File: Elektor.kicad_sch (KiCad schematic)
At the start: 55 parts, among them J1 Conn_Coaxial, J13 Conn_Coaxial, J6 Conn_01x03_Pin, J8 Conn_01x02, Q1 BF545B, U1 Si5351A-B-GT, U2 74HC04, U3 74HC4066D_653, U5 MCP6022, U6 AUDIOSHIELD-REVD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

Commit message: alternative layout first commit
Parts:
- added C20: 100n, Capacitor_SMD:C_0603_1608Metric, symbol Device:C
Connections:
- net GND: now also C20.2
- net at C16.1, R5.1, U2.14 (VCC)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: now also U2.1, U2.3, C20.1; no longer U2.11, U2.13
- net at U1.10 (CLK0), U3.5 (2E): now also U2.13; no longer U2.1
- net at U2.2: no longer U3.13 (1E)
- net at U1.9 (CLK1), U3.6 (3E): now also U2.11; no longer U2.3
- net at U2.4: no longer U3.12 (4E)
- net at U2.12: now also U3.13 (1E)
- net at U2.10: now also U3.12 (4E)
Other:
- moved on the sheet: U2A, U2B, U2E, U2F
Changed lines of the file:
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@@
   (junction (at 93.98 146.05) (diameter 0) (color 0 0 0 0)
   )
+  (junction (at 69.85 16.51) (diameter 0) (color 0 0 0 0)
+  )
+  (junction (at 123.19 130.81) (diameter 0) (color 0 0 0 0)
+  )
+  (junction (at 93.98 142.24) (diameter 0) (color 0 0 0 0)
+  )
+  (junction (at 215.9 115.57) (diameter 0) (color 0 0 0 0)
+  )
+  (junction (at 168.91 132.08) (diameter 0) (color 0 0 0 0)
+  )
+  (junction (at 115.57 146.05) (diameter 0) (color 0 0 0 0)
+  )
   (junction (at 109.22 40.64) (diameter 0) (color 0 0 0 0)
   )
-  (junction (at 69.85 16.51) (diameter 0) (color 0 0 0 0)
-  )
-  (junction (at 123.19 130.81) (diameter 0) (color 0 0 0 0)
-  )
-  (junction (at 93.98 142.24) (diameter 0) (color 0 0 0 0)
-  )
-  (junction (at 215.9 115.57) (diameter 0) (color 0 0 0 0)
-  )
-  (junction (at 168.91 132.08) (diameter 0) (color 0 0 0 0)
-  )
-  (junction (at 115.57 146.05) (diameter 0) (color 0 0 0 0)
-  )
   (junction (at 218.44 13.97) (diameter 0) (color 0 0 0 0)
   )
@@
   (junction (at 163.83 41.91) (diameter 0) (color 0 0 0 0)
   )
+  (junction (at 160.02 41.91) (diameter 0) (color 0 0 0 0)
+  )
   (junction (at 243.84 118.11) (diameter 0) (color 0 0 0 0)
   )
@@
   (junction (at 25.4 91.44) (diameter 0) (color 0 0 0 0)
   )
+  (junction (at 160.02 13.97) (diameter 0) (color 0 0 0 0)
+  )
   (junction (at 33.02 71.12) (diameter 0) (color 0 0 0 0)
   )
@@
     (stroke (width 0) (type default))
   )
-  (wire (pts (xy 151.13 41.91) (xy 163.83 41.91))
+  (wire (pts (xy 151.13 41.91) (xy 160.02 41.91))
     (stroke (width 0) (type default))
   )
@@
     (stroke (width 0) (type default))
   )
+  (wire (pts (xy 160.02 41.91) (xy 163.83 41.91))
+    (stroke (width 0) (type default))
+  )
   (wire (pts (xy 173.99 13.97) (xy 173.99 16.51))
     (stroke (width 0) (type default))
@@
     (stroke (width 0) (type default))
   )
+  (wire (pts (xy 160.02 13.97) (xy 160.02 21.59))
+    (stroke (width 0) (type default))
+  )
   (wire (pts (xy 223.52 144.78) (xy 223.52 147.32))
     (stroke (width 0) (type default))
@@
     (stroke (width 0) (type default))
   )
+  (wire (pts (xy 160.02 29.21) (xy 160.02 41.91))
+    (stroke (width 0) (type default))
+  )
   (wire (pts (xy 64.77 27.94) (xy 69.85 27.94))
     (stroke (width 0) (type default))
@@
     (stroke (width 0) (type default))
   )
+  (wire (pts (xy 160.02 13.97) (xy 173.99 13.97))
+    (stroke (width 0) (type default))
+  )
   (wire (pts (xy 115.57 129.54) (xy 115.57 130.81))
     (stroke (width 0) (type default))
@@
     (stroke (width 0) (type default))
   )
-  (wire (pts (xy 133.35 13.97) (xy 173.99 13.97))
+  (wire (pts (xy 133.35 13.97) (xy 160.02 13.97))
     (stroke (width 0) (type default))
   )
@@
     )
   )
+  (symbol (lib_id "Device:C") (at 160.02 25.4 0) (unit 1)
+    (in_bom yes) (on_board yes) (dnp no)
+    (property "Reference" "C20" (at 161.29 22.86 0)
+      (effects (font (size 1.27 1.27)) (justify left))
+    )
+    (property "Value" "100n" (at 161.29 27.94 0)
+      (effects (font (size 1.27 1.27)) (justify left))
+    )
+    (property "Footprint" "Capacitor_SMD:C_0603_1608Metric" (at 160.9852 29.21 0)
+      (effects (font (size 1.27 1.27)) hide)
+    )
+    (property "Datasheet" "~" (at 160.02 25.4 0)
+      (effects (font (size 1.27 1.27)) hide)
+    )
+    (pin "2")
+    (pin "1")
+    (instances
+      (project "Elektor"
+        (path "/d0df484f-6d39-4423-9bc6-c09d4efa8191"
+          (reference "C20") (unit 1)
+        )
+      )
+    )
+  )
   (symbol (lib_id "Device:R") (at 184.15 87.63 180) (unit 1)
     (in_bom yes) (on_board yes) (dnp no)
@@
     )
   )
-  (symbol (lib_id "74xx:74HC04") (at 116.84 40.64 0) (unit 1)
+  (symbol (lib_id "74xx:74HC04") (at 116.84 76.2 0) (unit 1)
     (in_bom yes) (on_board yes) (dnp no) (fields_autoplaced)
-    (property "Reference" "U2" (at 116.84 31.75 0)
-      (effects (font (size 1.27 1.27)))
-    )
-    (property "Value" "74HC04" (at 116.84 34.29 0)
-      (effects (font (size 1.27 1.27)))
-    )
-    (property "Footprint" "Package_SO:SOIC-14_3.9x8.7mm_P1.27mm" (at 116.84 40.64 0)
-      (effects (font (size 1.27 1.27)) hide)
-    )
-    (property "Datasheet" "https://assets.nexperia.com/documents/data-sheet/74HC_HCT04.pdf" (at 116.84 40.64 0)
+    (property "Reference" "U2" (at 116.84 67.31 0)
+      (effects (font (size 1.27 1.27)))
+    )
+    (property "Value" "74HC04" (at 116.84 69.85 0)
+      (effects (font (size 1.27 1.27)))
+    )
+    (property "Footprint" "Package_SO:SOIC-14_3.9x8.7mm_P1.27mm" (at 116.84 76.2 0)
+      (effects (font (size 1.27 1.27)) hide)
+    )
+    (property "Datasheet" "https://assets.nexperia.com/documents/data-sheet/74HC_HCT04.pdf" (at 116.84 76.2 0)
       (effects (font (size 1.27 1.27)) hide)
     )
@@
     )
   )
-  (symbol (lib_id "74xx:74HC04") (at 116.84 54.61 0) (unit 2)
+  (symbol (lib_id "74xx:74HC04") (at 116.84 78.74 0) (unit 2)
     (in_bom yes) (on_board yes) (dnp no) (fields_autoplaced)
-    (property "Reference" "U2" (at 116.84 45.72 0)
-      (effects (font (size 1.27 1.27)))
-    )
-    (property "Value" "74HC04" (at 116.84 48.26 0)
-      (effects (font (size 1.27 1.27)))
-    )
-    (property "Footprint" "Package_SO:SOIC-14_3.9x8.7mm_P1.27mm" (at 116.84 54.61 0)
-      (effects (font (size 1.27 1.27)) hide)
-    )
-    (property "Datasheet" "https://assets.nexperia.com/documents/data-sheet/74HC_HCT04.pdf" (at 116.84 54.61 0)
+    (property "Reference" "U2" (at 116.84 69.85 0)
+      (effects (font (size 1.27 1.27)))
+    )
+    (property "Value" "74HC04" (at 116.84 72.39 0)
+      (effects (font (size 1.27 1.27)))
+    )
+    (property "Footprint" "Package_SO:SOIC-14_3.9x8.7mm_P1.27mm" (at 116.84 78.74 0)
+      (effects (font (size 1.27 1.27)) hide)
+    )
+    (property "Datasheet" "https://assets.nexperia.com/documents/data-sheet/74HC_HCT04.pdf" (at 116.84 78.74 0)
       (effects (font (size 1.27 1.27)) hide)
     )
@@
   )
   (symbol (lib_id "74xx:74HC04") (at 173.99 29.21 0) (unit 7)
-    (in_bom yes) (on_board yes) (dnp no) (fields_autoplaced)
-    (property "Reference" "U2" (at 180.34 27.94 0)
-      (effects (font (size 1.27 1.27)) (justify left))
-    )
-    (property "Value" "74HC04" (at 180.34 30.48 0)
+    (in_bom yes) (on_board yes) (dnp no)
+    (property "Reference" "U2" (at 172.72 27.94 0)
+      (effects (font (size 1.27 1.27)) (justify left))
+    )
+    (property "Value" "74HC04" (at 170.18 30.48 0)
       (effects (font (size 1.27 1.27)) (justify left))
     )
@@
     )
   )
-  (symbol (lib_id "74xx:74HC04") (at 116.84 78.74 0) (unit 6)
+  (symbol (lib_id "74xx:74HC04") (at 116.84 40.64 0) (unit 6)
     (in_bom yes) (on_board yes) (dnp no) (fields_autoplaced)
-    (property "Reference" "U2" (at 116.84 69.85 0)
-      (effects (font (size 1.27 1.27)))
-    )
-    (property "Value" "74HC04" (at 116.84 72.39 0)
-      (effects (font (size 1.27 1.27)))
-    )
-    (property "Footprint" "Package_SO:SOIC-14_3.9x8.7mm_P1.27mm" (at 116.84 78.74 0)
-      (effects (font (size 1.27 1.27)) hide)
-    )
-    (property "Datasheet" "https://assets.nexperia.com/documents/data-sheet/74HC_HCT04.pdf" (at 116.84 78.74 0)
+    (property "Reference" "U2" (at 116.84 31.75 0)
+      (effects (font (size 1.27 1.27)))
+    )
+    (property "Value" "74HC04" (at 116.84 34.29 0)
+      (effects (font (size 1.27 1.27)))
+    )
+    (property "Footprint" "Package_SO:SOIC-14_3.9x8.7mm_P1.27mm" (at 116.84 40.64 0)
+      (effects (font (size 1.27 1.27)) hide)
+    )
+    (property "Datasheet" "https://assets.nexperia.com/documents/data-sheet/74HC_HCT04.pdf" (at 116.84 40.64 0)
       (effects (font (size 1.27 1.27)) hide)
     )
@@
     )
   )
-  (symbol (lib_id "74xx:74HC04") (at 116.84 76.2 0) (unit 5)
+  (symbol (lib_id "74xx:74HC04") (at 116.84 54.61 0) (unit 5)
     (in_bom yes) (on_board yes) (dnp no) (fields_autoplaced)
-    (property "Reference" "U2" (at 116.84 67.31 0)
-      (effects (font (size 1.27 1.27)))
-    )
-    (property "Value" "74HC04" (at 116.84 69.85 0)
-      (effects (font (size 1.27 1.27)))
-    )
-    (property "Footprint" "Package_SO:SOIC-14_3.9x8.7mm_P1.27mm" (at 116.84 76.2 0)
-      (effects (font (size 1.27 1.27)) hide)
-    )
-    (property "Datasheet" "https://assets.nexperia.com/documents/data-sheet/74HC_HCT04.pdf" (at 116.84 76.2 0)
-      (effects (font (size 1.27 1.27)) hide)
-    )
+    (property "Reference" "U2" (at 116.84 45.72 0)
+      (effects (font (size 1.27 1.27)))
+    )
+    (property "Value" "74HC04" (at 116.84 48.26 0)
+      (effects (font (size 1.27 1.27)))
+    )
+    (property "Footprint" "Package_SO:SOIC-14_3.9x8.7mm_P1.27mm" (at 116.84 54.61 0)
+      (effects (font (size 1.27 1.27)) hide)
+    )
+    (property "Datasheet" "https://assets.nexperia.com/documents/data-sheet/74HC_HCT04.pdf" (at 116.84 54.61 0)
+      (effects (font (size 1.27 1.27)) hide)
+    )

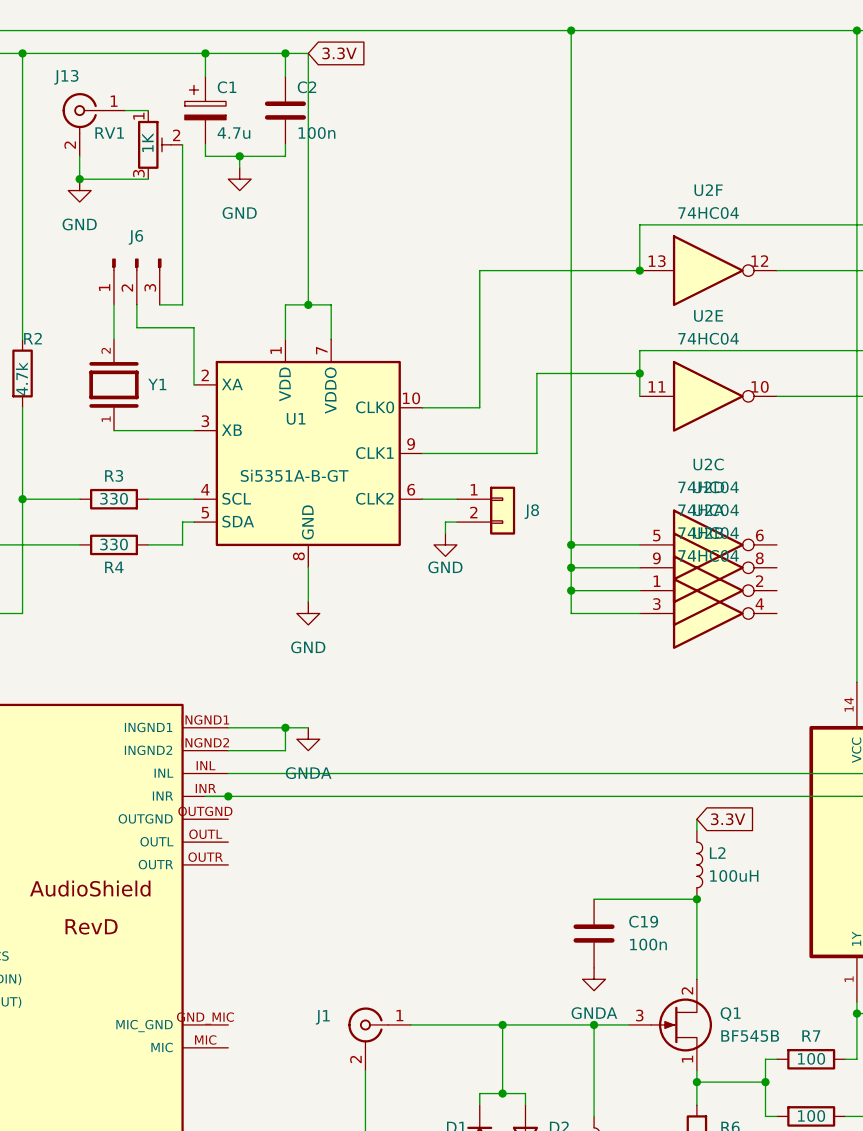
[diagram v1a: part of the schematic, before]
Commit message: decouplages, capa de liaison generateur externe, marges de prehension, trous de fixations
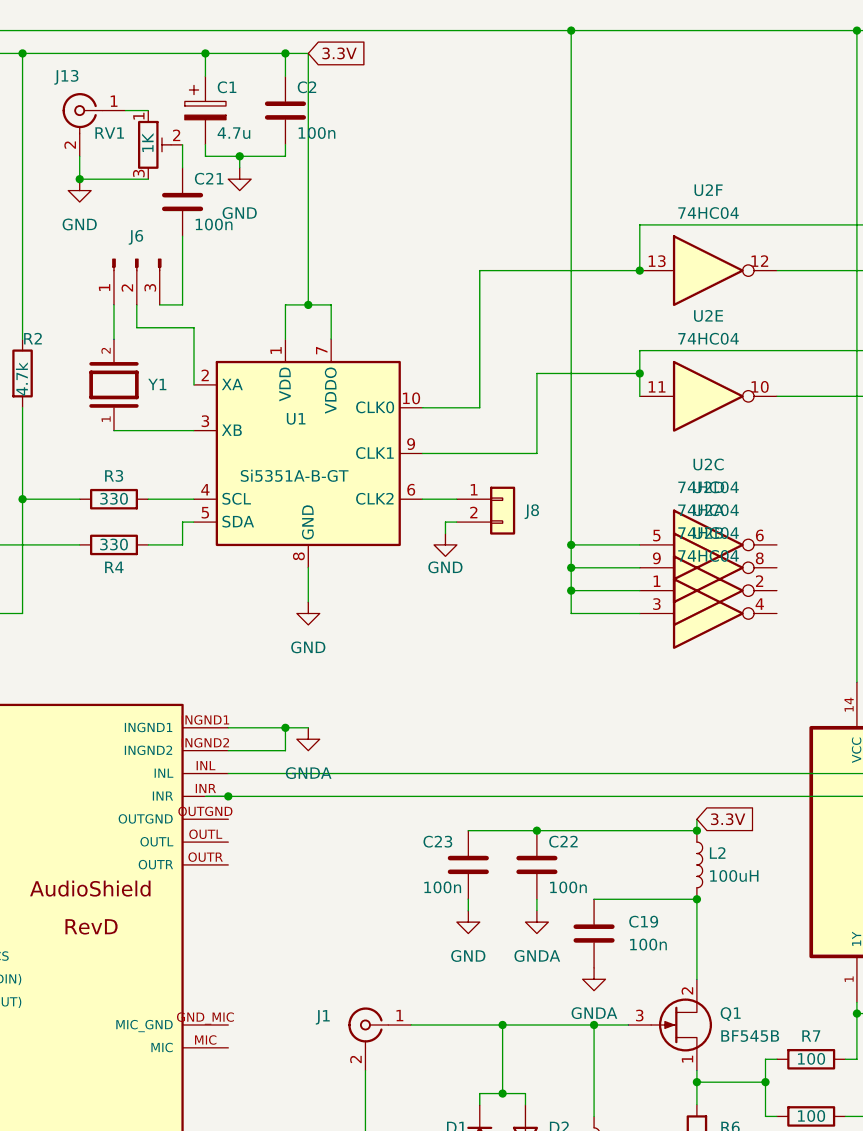
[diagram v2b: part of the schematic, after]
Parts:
- added C21, C22, C23: 100n, Capacitor_SMD:C_0603_1608Metric, symbol Device:C
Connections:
- net 3.3V: now also C22.1, C23.1
- net GND: now also C23.2
- net GNDA: now also C22.2
- net at RV1.2: now also C21.1; no longer J6.3 (Pin_3)
- new net: C21.2, J6.3 (Pin_3)
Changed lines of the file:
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@@
   (junction (at 199.39 13.97) (diameter 0) (color 0 0 0 0)
   )
+  (junction (at 97.79 102.87) (diameter 0) (color 0 0 0 0)
+  )
   (junction (at 199.39 41.91) (diameter 0) (color 0 0 0 0)
   )
@@
   (junction (at 93.98 146.05) (diameter 0) (color 0 0 0 0)
   )
+  (junction (at 115.57 102.87) (diameter 0) (color 0 0 0 0)
+  )
   (junction (at 69.85 16.51) (diameter 0) (color 0 0 0 0)
   )
@@
     (stroke (width 0) (type default))
   )
+  (wire (pts (xy 97.79 110.49) (xy 97.79 111.76))
+    (stroke (width 0) (type default))
+  )
   (wire (pts (xy 151.13 41.91) (xy 160.02 41.91))
     (stroke (width 0) (type default))
@@
     (stroke (width 0) (type default))
   )
+  (wire (pts (xy 90.17 102.87) (xy 97.79 102.87))
+    (stroke (width 0) (type default))
+  )
   (wire (pts (xy 50.8 44.45) (xy 50.8 48.26))
     (stroke (width 0) (type default))
@@
     (stroke (width 0) (type default))
   )
+  (wire (pts (xy 58.42 36.83) (xy 58.42 44.45))
+    (stroke (width 0) (type default))
+  )
   (wire (pts (xy 199.39 31.75) (xy 199.39 41.91))
     (stroke (width 0) (type default))
@@
     (stroke (width 0) (type default))
   )
+  (wire (pts (xy 97.79 102.87) (xy 115.57 102.87))
+    (stroke (width 0) (type default))
+  )
   (wire (pts (xy 91.44 132.08) (xy 91.44 133.35))
     (stroke (width 0) (type default))
@@
     (stroke (width 0) (type default))
   )
+  (wire (pts (xy 58.42 26.67) (xy 58.42 29.21))
+    (stroke (width 0) (type default))
+  )
   (wire (pts (xy 24.13 78.74) (xy 24.13 147.32))
     (stroke (width 0) (type default))
@@
     (stroke (width 0) (type default))
   )
-  (wire (pts (xy 58.42 26.67) (xy 58.42 44.45))
+  (wire (pts (xy 90.17 110.49) (xy 90.17 111.76))
     (stroke (width 0) (type default))
   )
@@
     )
   )
+  (symbol (lib_id "Device:C") (at 90.17 106.68 0) (unit 1)
+    (in_bom yes) (on_board yes) (dnp no)
+    (property "Reference" "C23" (at 85.09 104.14 0)
+      (effects (font (size 1.27 1.27)) (justify left))
+    )
+    (property "Value" "100n" (at 85.09 109.22 0)
+      (effects (font (size 1.27 1.27)) (justify left))
+    )
+    (property "Footprint" "Capacitor_SMD:C_0603_1608Metric" (at 91.1352 110.49 0)
+      (effects (font (size 1.27 1.27)) hide)
+    )
+    (property "Datasheet" "~" (at 90.17 106.68 0)
+      (effects (font (size 1.27 1.27)) hide)
+    )
+    (pin "2")
+    (pin "1")
+    (instances
+      (project "Elektor"
+        (path "/d0df484f-6d39-4423-9bc6-c09d4efa8191"
+          (reference "C23") (unit 1)
+        )
+      )
+    )
+  )
   (symbol (lib_id "74xx:74HC04") (at 116.84 76.2 0) (unit 1)
     (in_bom yes) (on_board yes) (dnp no) (fields_autoplaced)
@@
     )
   )
+  (symbol (lib_id "power:GND") (at 90.17 111.76 0) (unit 1)
+    (in_bom yes) (on_board yes) (dnp no) (fields_autoplaced)
+    (property "Reference" "#PWR016" (at 90.17 118.11 0)
+      (effects (font (size 1.27 1.27)) hide)
+    )
+    (property "Value" "GND" (at 90.17 116.84 0)
+      (effects (font (size 1.27 1.27)))
+    )
+    (property "Footprint" "" (at 90.17 111.76 0)
+      (effects (font (size 1.27 1.27)) hide)
+    )
+    (property "Datasheet" "" (at 90.17 111.76 0)
+      (effects (font (size 1.27 1.27)) hide)
+    )
+    (pin "1")
+    (instances
+      (project "Elektor"
+        (path "/d0df484f-6d39-4423-9bc6-c09d4efa8191"
+          (reference "#PWR016") (unit 1)
+        )
+      )
+    )
+  )
   (symbol (lib_id "Device:C_Polarized") (at 218.44 25.4 0) (unit 1)
     (in_bom yes) (on_board yes) (dnp no)
@@
     )
   )
+  (symbol (lib_id "power:GNDA") (at 97.79 111.76 0) (unit 1)
+    (in_bom yes) (on_board yes) (dnp no) (fields_autoplaced)
+    (property "Reference" "#PWR011" (at 97.79 118.11 0)
+      (effects (font (size 1.27 1.27)) hide)
+    )
+    (property "Value" "GNDA" (at 97.79 116.84 0)
+      (effects (font (size 1.27 1.27)))
+    )
+    (property "Footprint" "" (at 97.79 111.76 0)
+      (effects (font (size 1.27 1.27)) hide)
+    )
+    (property "Datasheet" "" (at 97.79 111.76 0)
+      (effects (font (size 1.27 1.27)) hide)
+    )
+    (pin "1")
+    (instances
+      (project "Elektor"
+        (path "/d0df484f-6d39-4423-9bc6-c09d4efa8191"
+          (reference "#PWR011") (unit 1)
+        )
+      )
+    )
+  )
   (symbol (lib_id "Device:R") (at 233.68 73.66 90) (unit 1)
     (in_bom yes) (on_board yes) (dnp no)
@@
     )
   )
+  (symbol (lib_id "Device:C") (at 97.79 106.68 0) (unit 1)
+    (in_bom yes) (on_board yes) (dnp no)
+    (property "Reference" "C22" (at 99.06 104.14 0)
+      (effects (font (size 1.27 1.27)) (justify left))
+    )
+    (property "Value" "100n" (at 99.06 109.22 0)
+      (effects (font (size 1.27 1.27)) (justify left))
+    )
+    (property "Footprint" "Capacitor_SMD:C_0603_1608Metric" (at 98.7552 110.49 0)
+      (effects (font (size 1.27 1.27)) hide)
+    )
+    (property "Datasheet" "~" (at 97.79 106.68 0)
+      (effects (font (size 1.27 1.27)) hide)
+    )
+    (pin "2")
+    (pin "1")
+    (instances
+      (project "Elektor"
+        (path "/d0df484f-6d39-4423-9bc6-c09d4efa8191"
+          (reference "C22") (unit 1)
+        )
+      )
+    )
+  )
   (symbol (lib_id "74xx:74HC04") (at 116.84 54.61 0) (unit 5)
     (in_bom yes) (on_board yes) (dnp no) (fields_autoplaced)
@@
         )
       )
+    )
+  )
+  (symbol (lib_id "Device:C") (at 58.42 33.02 0) (unit 1)
+    (in_bom yes) (on_board yes) (dnp no)
+    (property "Reference" "C21" (at 59.69 30.48 0)
+      (effects (font (size 1.27 1.27)) (justify left))
+    )
+    (property "Value" "100n" (at 59.69 35.56 0)
+      (effects (font (size 1.27 1.27)) (justify left))
+    )
+    (property "Footprint" "Capacitor_SMD:C_0603_1608Metric" (at 59.3852 36.83 0)
+      (effects (font (size 1.27 1.27)) hide)
+    )
+    (property "Datasheet" "~" (at 58.42 33.02 0)
+      (effects (font (size 1.27 1.27)) hide)
+    )
+    (pin "2")
+    (pin "1")
+    (instances
+      (project "Elektor"
+        (path "/d0df484f-6d39-4423-9bc6-c09d4efa8191"
+          (reference "C21") (unit 1)
+        )
+      )
